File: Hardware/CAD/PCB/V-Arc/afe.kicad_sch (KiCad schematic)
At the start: 10 parts, among them J3 AudioJack2, SW1 SW_SPDT, U5 TL072

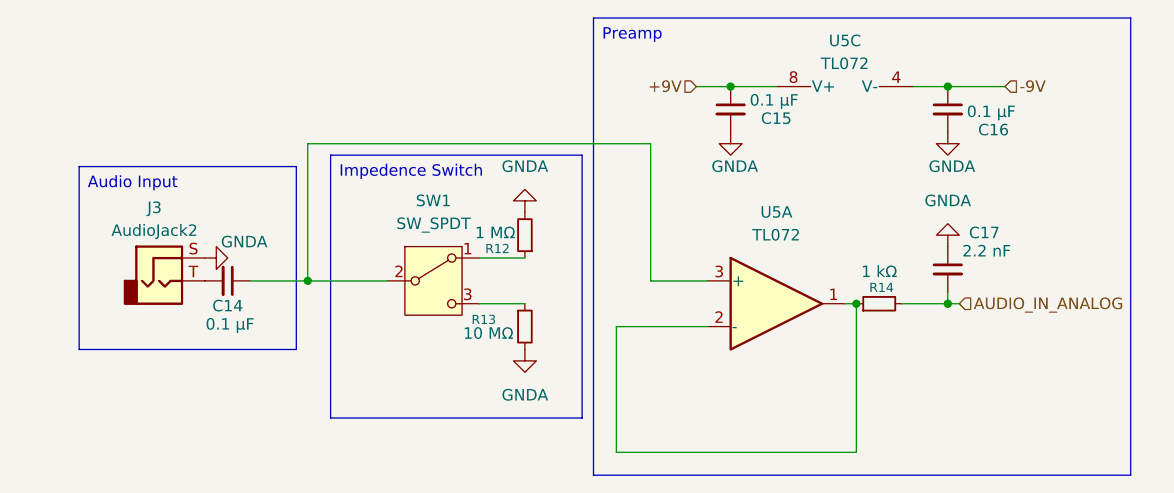
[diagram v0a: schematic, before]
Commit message: Assigned Footprints
-Swapped input jack to a switched one
-Assigned footprints for all items
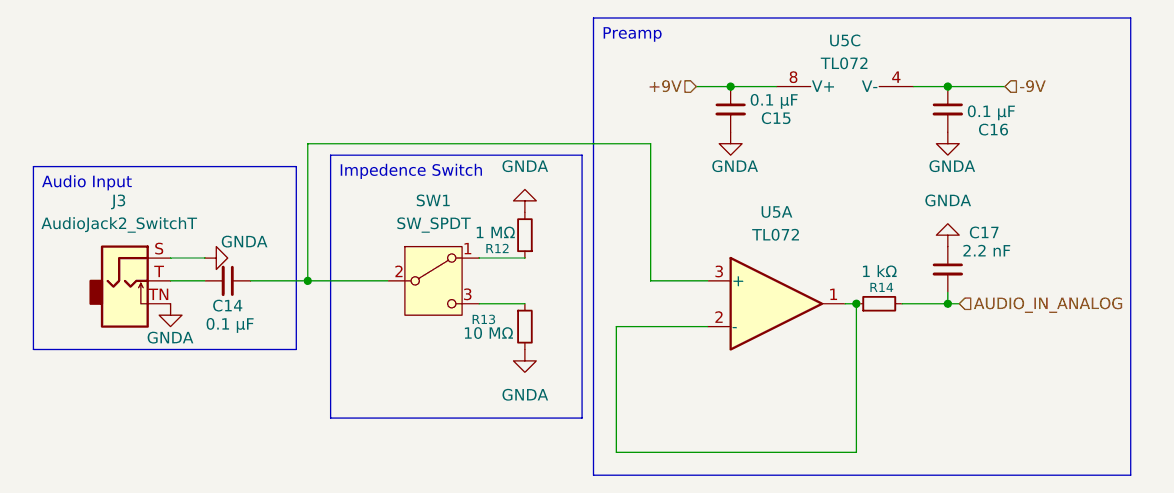
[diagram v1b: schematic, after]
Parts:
- removed J3: AudioJack2, symbol Connector_Audio:AudioJack2
- added J3: AudioJack2_SwitchT, Connector_Audio:Jack_3.5mm_CUI_SJ1-3513N_Horizontal, symbol Connector_Audio:AudioJack2_SwitchT
- C14, C15, C16, C17: footprint (none) -> Capacitor_SMD:C_0805_2012Metric
- R12, R13, R14: footprint (none) -> Resistor_SMD:R_0805_2012Metric
- SW1: footprint (none) -> Button_Switch_THT:SW_PUSH_6mm
- U5: footprint (none) -> Package_SO:SOIC-8_3.9x4.9mm_P1.27mm
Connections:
- net GNDA: now also J3.S, J3.TN
- net at C14.2: now also J3.T
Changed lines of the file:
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@@
 	(text_box "Audio Input"
 		(exclude_from_sim no)
-		(at 77.47 90.17 0)
-		(size 24.13 20.32)
+		(at 72.39 90.17 0)
+		(size 29.21 20.32)
 		(margins 0.9525 0.9525 0.9525 0.9525)
 		(stroke
@@
 	(wire
 		(pts
+			(xy 87.63 102.87) (xy 91.44 102.87)
+		)
+		(stroke
+			(width 0)
+			(type default)
+		)
+	)
+	(wire
+		(pts
 			(xy 173.99 105.41) (xy 175.26 105.41)
 		)
@@
 			(type default)
 			(color 255 0 4 1)
+		)
+	)
+	(wire
+		(pts
+			(xy 87.63 100.33) (xy 91.44 100.33)
+		)
+		(stroke
+			(width 0)
+			(type default)
 		)
 	)
@@
 	)
 	(symbol
+		(lib_id "Connector_Audio:AudioJack2_SwitchT")
+		(at 82.55 102.87 0)
+		(unit 1)
+		(body_style 1)
+		(exclude_from_sim no)
+		(in_bom yes)
+		(on_board yes)
+		(in_pos_files yes)
+		(dnp no)
+		(fields_autoplaced yes)
+		(property "Reference" "J3"
+			(at 81.915 93.98 0)
+			(show_name no)
+			(do_not_autoplace no)
+			(effects
+				(font
+					(size 1.27 1.27)
+				)
+			)
+		)
+		(property "Value" "AudioJack2_SwitchT"
+			(at 81.915 96.52 0)
+			(show_name no)
+			(do_not_autoplace no)
+			(effects
+				(font
+					(size 1.27 1.27)
+				)
+			)
+		)
+		(property "Footprint" "Connector_Audio:Jack_3.5mm_CUI_SJ1-3513N_Horizontal"
+			(at 82.55 102.87 0)
+			(hide yes)
+			(show_name no)
+			(do_not_autoplace no)
+			(effects
+				(font
+					(size 1.27 1.27)
+				)
+			)
+		)
+		(property "Datasheet" ""
+			(at 82.55 102.87 0)
+			(hide yes)
+			(show_name no)
+			(do_not_autoplace no)
+			(effects
+				(font
+					(size 1.27 1.27)
+				)
+			)
+		)
+		(property "Description" "Audio Jack, 2 Poles (Mono / TS), Switched T Pole (Normalling)"
+			(at 82.55 102.87 0)
+			(hide yes)
+			(show_name no)
+			(do_not_autoplace no)
+			(effects
+				(font
+					(size 1.27 1.27)
+				)
+			)
+		)
+		(pin "T"
+		)
+		(pin "S"
+		)
+		(pin "TN"
+		)
+		(instances
+			(project "V-Arc"
+				(path "/c2c0cba2-f358-4c92-8083-c3d5939961a9/895d23e7-783f-4f78-956b-f477f8052eec"
+					(reference "J3")
+					(unit 1)
+				)
+			)
+		)
+	)
+	(symbol
 		(lib_id "Device:C_Small")
 		(at 93.98 102.87 270)
@@
 			)
 		)
-		(property "Footprint" ""
+		(property "Footprint" "Capacitor_SMD:C_0805_2012Metric"
 			(at 93.98 102.87 0)
 			(hide yes)
@@
 			)
 		)
-		(property "Footprint" ""
+		(property "Footprint" "Capacitor_SMD:C_0805_2012Metric"
 			(at 149.86 83.82 0)
 			(hide yes)
@@
 			)
 		)
-		(property "Footprint" ""
+		(property "Footprint" "Resistor_SMD:R_0805_2012Metric"
 			(at 127 97.79 0)
 			(hide yes)
@@
 			)
 		)
-		(property "Footprint" ""
+		(property "Footprint" "Button_Switch_THT:SW_PUSH_6mm"
 			(at 116.84 102.87 0)
 			(hide yes)
@@
 			)
 		)
-		(property "Footprint" ""
+		(property "Footprint" "Capacitor_SMD:C_0805_2012Metric"
 			(at 173.99 83.82 0)
 			(hide yes)
@@
 			)
 		)
-		(property "Footprint" ""
+		(property "Footprint" "Capacitor_SMD:C_0805_2012Metric"
 			(at 173.99 101.6 0)
 			(hide yes)
@@
 			)
 		)
-		(property "Footprint" ""
+		(property "Footprint" "Package_SO:SOIC-8_3.9x4.9mm_P1.27mm"
 			(at 162.56 78.74 0)
 			(hide yes)
@@
 	)
 	(symbol
-		(lib_id "Connector_Audio:AudioJack2")
-		(at 86.36 102.87 0)
-		(unit 1)
-		(body_style 1)
-		(exclude_from_sim no)
-		(in_bom yes)
-		(on_board yes)
-		(in_pos_files yes)
-		(dnp no)
-		(property "Reference" "J3"
-			(at 85.852 94.742 0)
-			(show_name no)
-			(do_not_autoplace no)
-			(effects
-				(font
-					(size 1.27 1.27)
-				)
-			)
-		)
-		(property "Value" "AudioJack2"
-			(at 85.852 97.282 0)
-			(show_name no)
-			(do_not_autoplace no)
-			(effects
-				(font
-					(size 1.27 1.27)
-				)
-			)
-		)
-		(property "Footprint" ""
-			(at 86.36 102.87 0)
-			(hide yes)
-			(show_name no)
-			(do_not_autoplace no)
-			(effects
-				(font
-					(size 1.27 1.27)
-				)
-			)
-		)
-		(property "Datasheet" ""
-			(at 86.36 102.87 0)
-			(hide yes)
-			(show_name no)
-			(do_not_autoplace no)
-			(effects
-				(font
-					(size 1.27 1.27)
-				)
-			)
-		)
-		(property "Description" "Audio Jack, 2 Poles (Mono / TS)"
-			(at 86.36 102.87 0)
-			(hide yes)
-			(show_name no)
-			(do_not_autoplace no)
-			(effects
-				(font
-					(size 1.27 1.27)
-				)
-			)
-		)
-		(pin "S"
-		)
-		(pin "T"
-		)
-		(instances
-			(project "V-Arc"
-				(path "/c2c0cba2-f358-4c92-8083-c3d5939961a9/895d23e7-783f-4f78-956b-f477f8052eec"
-					(reference "J3")
-					(unit 1)
-				)
-			)
-		)
-	)
-	(symbol
 		(lib_id "Amplifier_Operational:TL072")
 		(at 154.94 105.41 0)
@@
 			)
 		)
-		(property "Footprint" ""
+		(property "Footprint" "Package_SO:SOIC-8_3.9x4.9mm_P1.27mm"
 			(at 154.94 105.41 0)
 			(hide yes)
@@
 			)
 		)
-		(property "Footprint" ""
+		(property "Footprint" "Resistor_SMD:R_0805_2012Metric"
 			(at 166.37 105.41 0)
 			(hide yes)
@@
 	(symbol
 		(lib_id "power:GNDA")
+		(at 87.63 105.41 0)
+		(unit 1)
+		(body_style 1)
+		(exclude_from_sim no)
+		(in_bom yes)
+		(on_board yes)
+		(in_pos_files yes)
+		(dnp no)
+		(property "Reference" "#PWR041"
+			(at 87.63 111.76 0)
+			(hide yes)
+			(show_name no)
+			(do_not_autoplace no)
+			(effects
+				(font
+					(size 1.27 1.27)
+				)
+			)
+		)
+		(property "Value" "GNDA"
+			(at 90.17 109.22 0)
+			(show_name no)
+			(do_not_autoplace no)
+			(effects
+				(font
+					(size 1.27 1.27)
+				)
+				(justify right)
+			)
+		)
+		(property "Footprint" ""
+			(at 87.63 105.41 0)
+			(hide yes)
+			(show_name no)
+			(do_not_autoplace no)
+			(effects
+				(font
+					(size 1.27 1.27)
+				)
+			)
+		)
+		(property "Datasheet" ""
+			(at 87.63 105.41 0)
+			(hide yes)
+			(show_name no)
+			(do_not_autoplace no)
+			(effects
+				(font
+					(size 1.27 1.27)
+				)
+			)
+		)
+		(property "Description" "Power symbol creates a global label with name \"GNDA\" , analog ground"
+			(at 87.63 105.41 0)
+			(hide yes)
+			(show_name no)
+			(do_not_autoplace no)
+			(effects
+				(font
+					(size 1.27 1.27)
+				)
+			)
+		)
+		(pin "1"
+		)
+		(instances
+			(project "V-Arc"
+				(path "/c2c0cba2-f358-4c92-8083-c3d5939961a9/895d23e7-783f-4f78-956b-f477f8052eec"
+					(reference "#PWR041")
+					(unit 1)
+				)
+			)
+		)
+	)
+	(symbol
+		(lib_id "power:GNDA")
 		(at 173.99 86.36 0)
 		(unit 1)
@@
 			)
 		)
-		(property "Footprint" ""
+		(property "Footprint" "Resistor_SMD:R_0805_2012Metric"
 			(at 127 107.95 0)
 			(hide yes)

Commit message: Started PCB
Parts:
- C14: footprint Capacitor_SMD:C_0805_2012Metric -> Capacitor_SMD:CP_Elec_6.3x5.4
- SW1: footprint Button_Switch_THT:SW_PUSH_6mm -> Button_Switch_THT:SW_Slide_SPDT_Straight_CK_OS102011MS2Q
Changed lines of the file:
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@@
 			)
 		)
-		(property "Footprint" "Capacitor_SMD:C_0805_2012Metric"
+		(property "Footprint" "Capacitor_SMD:CP_Elec_6.3x5.4"
 			(at 93.98 102.87 0)
 			(hide yes)
@@
 			)
 		)
-		(property "Footprint" "Button_Switch_THT:SW_PUSH_6mm"
+		(property "Footprint" "Button_Switch_THT:SW_Slide_SPDT_Straight_CK_OS102011MS2Q"
 			(at 116.84 102.87 0)
 			(hide yes)

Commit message: Added BOM
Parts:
- C14: footprint Capacitor_SMD:CP_Elec_6.3x5.4 -> Capacitor_SMD:C_0805_2012Metric
- J3: footprint Connector_Audio:Jack_3.5mm_CUI_SJ1-3513N_Horizontal -> Connector_Audio:Jack_6.35mm_Neutrik_NMJ4HCD2_Horizontal
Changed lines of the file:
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@@
 			)
 		)
-		(property "Footprint" "Connector_Audio:Jack_3.5mm_CUI_SJ1-3513N_Horizontal"
+		(property "Footprint" "Connector_Audio:Jack_6.35mm_Neutrik_NMJ4HCD2_Horizontal"
 			(at 82.55 102.87 0)
 			(hide yes)
@@
 			)
 		)
-		(property "Footprint" "Capacitor_SMD:CP_Elec_6.3x5.4"
+		(property "Footprint" "Capacitor_SMD:C_0805_2012Metric"
 			(at 93.98 102.87 0)
 			(hide yes)
